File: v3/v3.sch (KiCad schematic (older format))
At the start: 52 parts

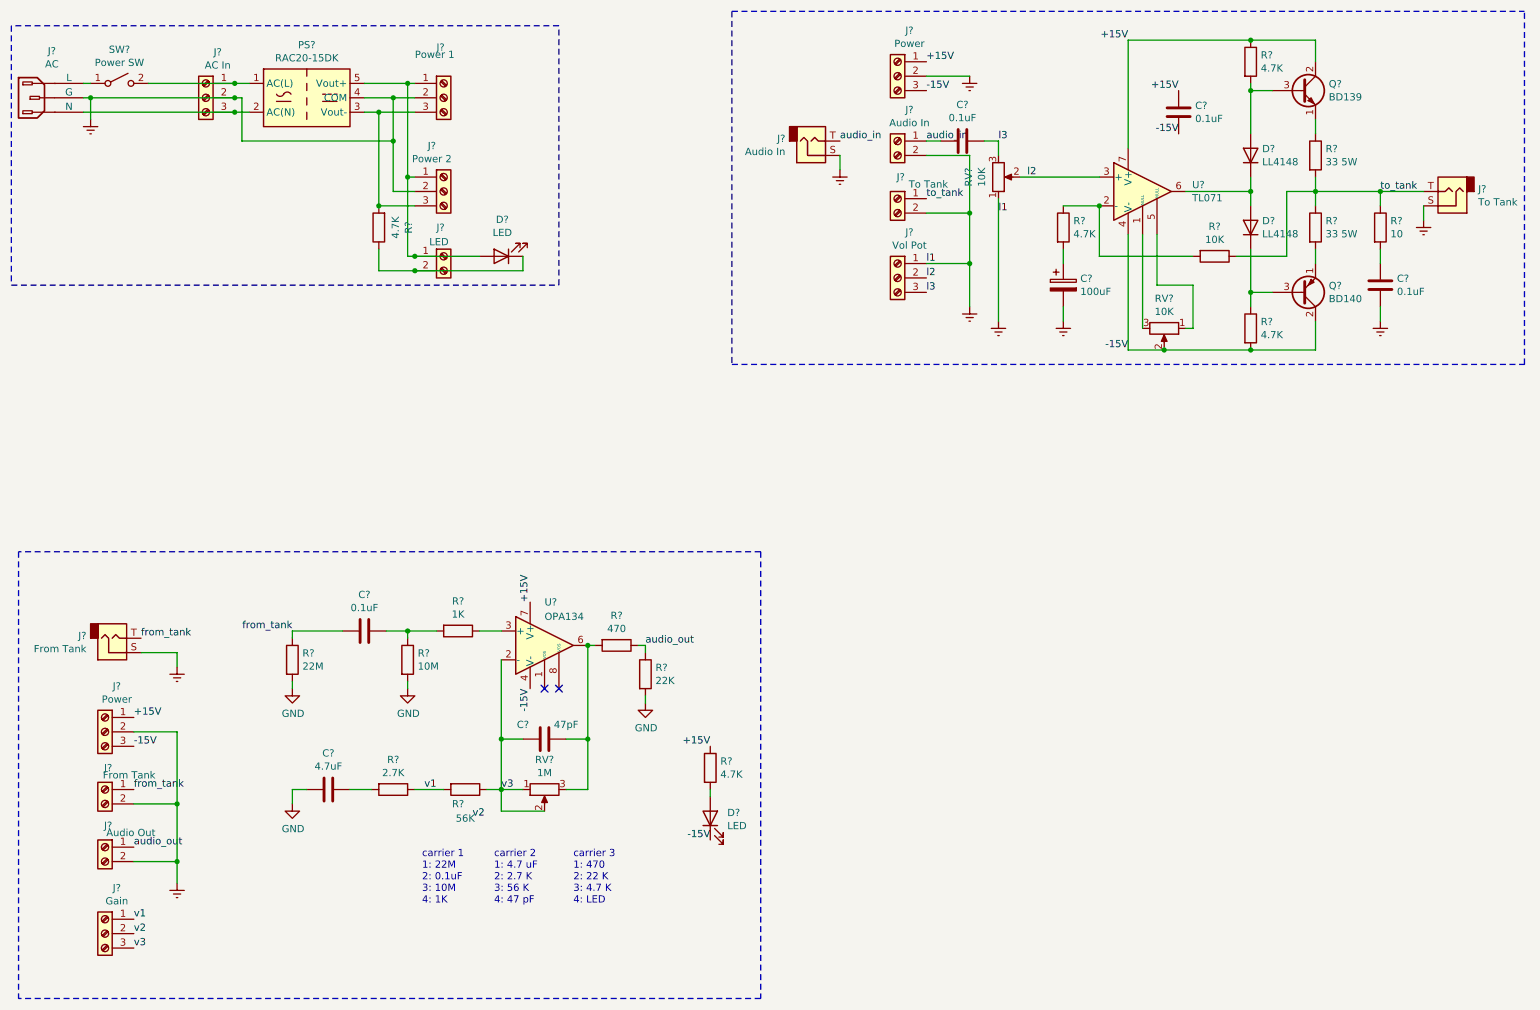
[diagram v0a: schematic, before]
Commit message: add pcb and cad model for the power supply module
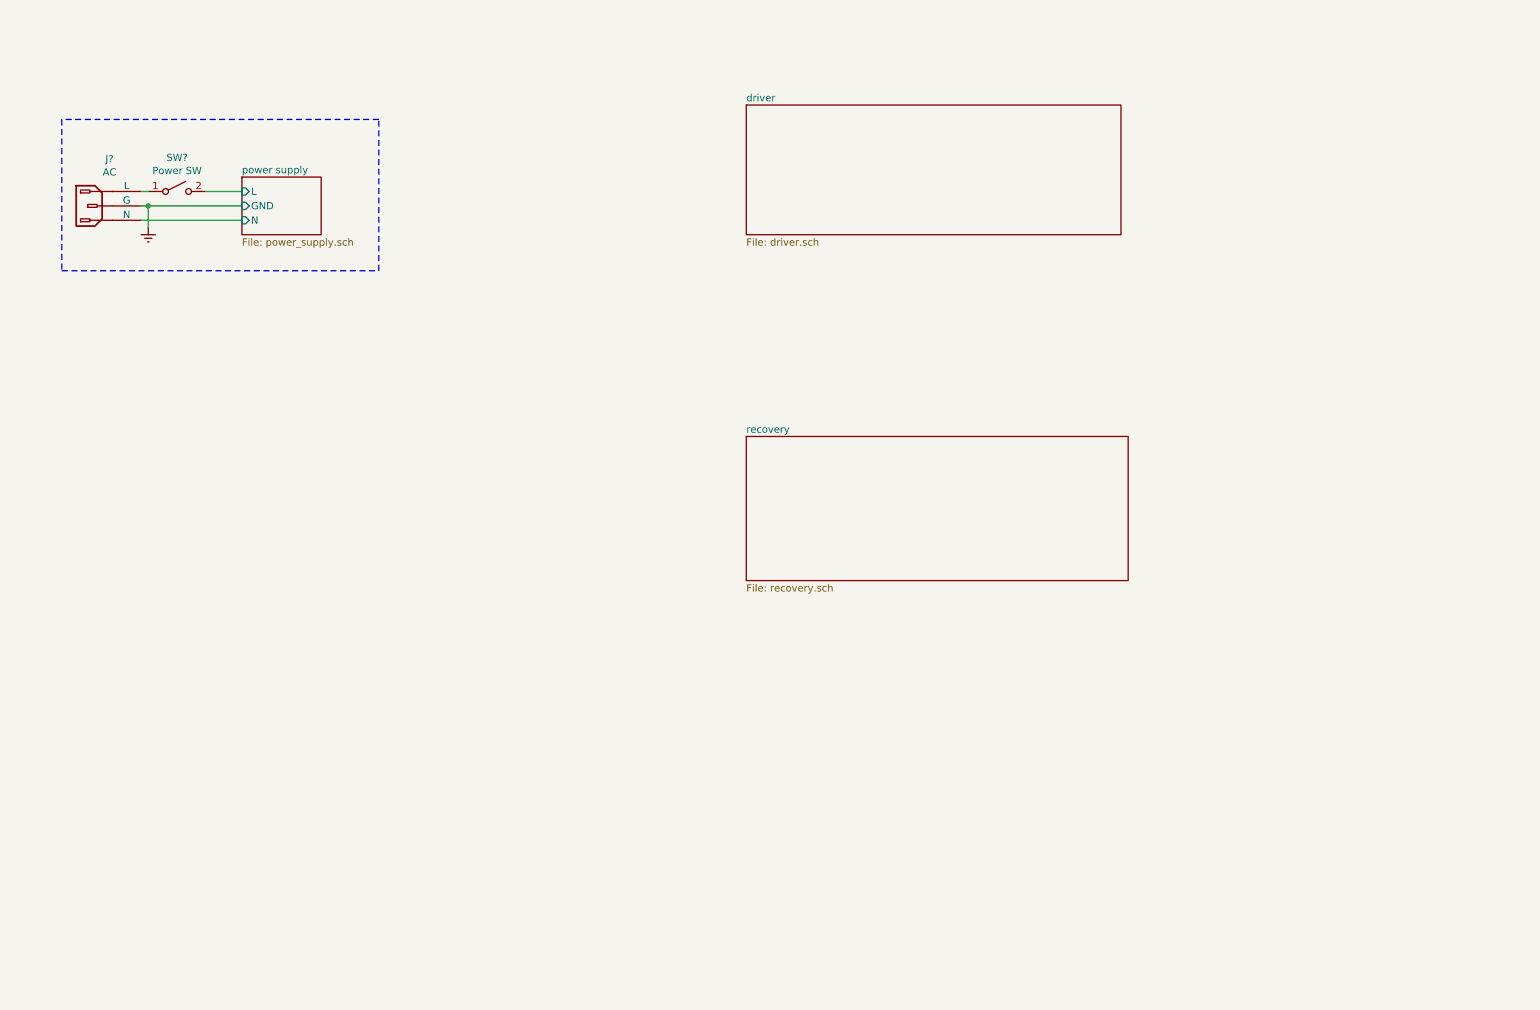
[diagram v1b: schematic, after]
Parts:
- removed C? (x3): 0.1uF, symbol Device:C
- removed C?: 100uF, symbol Device:CP
- removed C?: 47pF, Capacitor_SMD:C_0603_1608Metric, symbol Device:C
- removed C?: 4.7uF, Capacitor_SMD:C_0603_1608Metric, symbol Device:C
- removed C?: 0.1uF, Capacitor_SMD:C_0603_1608Metric, symbol Device:C
- removed D? (x2): LED, symbol Device:LED
- removed D? (x2): LL4148, Diode_SMD:D_MiniMELF, symbol Diode:LL4148
- removed J?: Power 2, symbol Connector:Screw_Terminal_01x03
- removed J?: LED, symbol Connector:Screw_Terminal_01x02
- removed J?: AC In, TerminalBlock_WAGO:TerminalBlock_WAGO_236-103_1x03_P5.00mm_45Degree, symbol Connector:Screw_Terminal_01x03
- removed J?: Power 1, TerminalBlock_TE-Connectivity:TerminalBlock_TE_282834-3_1x03_P2.54mm_Horizontal, symbol Connector:Screw_Terminal_01x03
- removed J?: Audio In, symbol Connector:AudioJack2
- removed J?: Audio In, symbol Connector:Screw_Terminal_01x02
- removed J?: To Tank, symbol Connector:AudioJack2
- removed J?: To Tank, symbol Connector:Screw_Terminal_01x02
- removed J? (x2): Power, symbol Connector:Screw_Terminal_01x03
- removed J?: Vol Pot, symbol Connector:Screw_Terminal_01x03
- removed J?: From Tank, symbol Connector:AudioJack2
- removed J?: From Tank, symbol Connector:Screw_Terminal_01x02
- removed J?: Audio Out, symbol Connector:Screw_Terminal_01x02
- removed J?: Gain, symbol Connector:Screw_Terminal_01x03
- removed PS?: RAC20-15DK, local:Converter_ACDC_RECOM_RAC05-xxSK_THT, symbol local:RAC20-15DK
- removed Q?: BD139, Package_TO_SOT_THT:TO-126-3_Vertical, symbol Transistor_BJT:BD139
- removed Q?: BD140, Package_TO_SOT_THT:TO-126-3_Vertical, symbol Transistor_BJT:BD140
- removed R? (x2): 4.7K, symbol Device:R
- removed R? (x3): 4.7K, Resistor_SMD:R_0603_1608Metric, symbol Device:R
- removed R?: 10K, symbol Device:R
- removed R? (x2): 33 5W, symbol Device:R
- removed R?: 10, Resistor_SMD:R_0603_1608Metric, symbol Device:R
- removed R?: 1K, Resistor_SMD:R_0603_1608Metric, symbol Device:R
- removed R?: 10M, Resistor_SMD:R_0603_1608Metric, symbol Device:R
- removed R?: 56K, Resistor_SMD:R_0603_1608Metric, symbol Device:R
- removed R?: 2.7K, Resistor_SMD:R_0603_1608Metric, symbol Device:R
- removed R?: 22M, Resistor_SMD:R_0603_1608Metric, symbol Device:R
- removed R?: 470, Resistor_SMD:R_0603_1608Metric, symbol Device:R
- removed R?: 22K, Resistor_SMD:R_0603_1608Metric, symbol Device:R
- removed RV? (x2): 10K, symbol Device:R_POT
- removed RV?: 1M, symbol Device:R_POT
- removed U?: TL071, Package_SO:SO-8_3.9x4.9mm_P1.27mm, symbol Amplifier_Operational:TL071
- removed U?: OPA134, Package_SO:SOIC-8_3.9x4.9mm_P1.27mm, symbol Amplifier_Operational:OPA134
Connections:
- net power supply/N: now reaches J?.~ (N)
- net power supply/L: now reaches SW?.2 (B)
- no-connect marks 2 -> 0
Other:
- note removed: "carrier 1\n1: 22M\n2: 0.1uF\n3: 10M\n4: 1K"
- note removed: "carrier 2\n1: 4.7 uF\n2: 2.7 K\n3: 56 K\n4: 47 pF"
- note removed: "carrier 3\n1: 470\n2: 22 K\n3: 4.7 K\n4: LED"
- moved on the sheet: J?, SW?
